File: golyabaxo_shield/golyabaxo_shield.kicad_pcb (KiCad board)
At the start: 2 copper layers, 53.6 x 54 mm, 18 parts, among them J2 Conn_01x09, Q2 Q_NPN_BEC

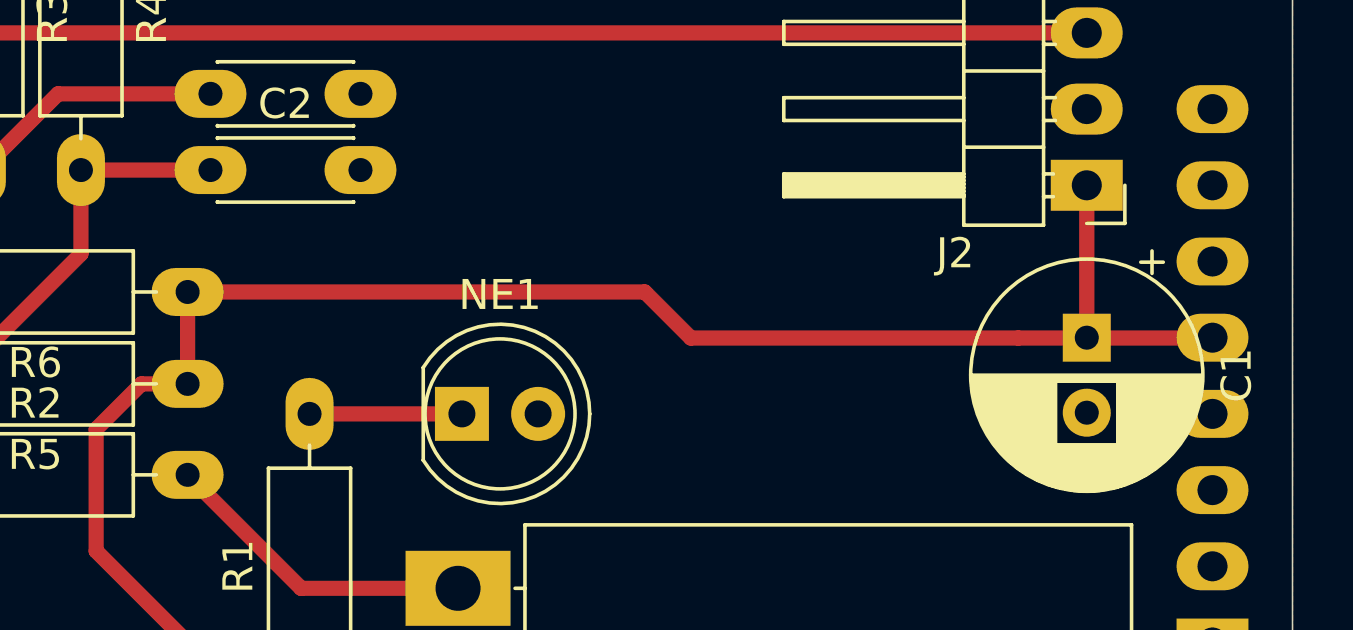
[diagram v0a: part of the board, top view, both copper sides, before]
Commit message: Add refurbished firmware for SEMduino-V2 - testing needed
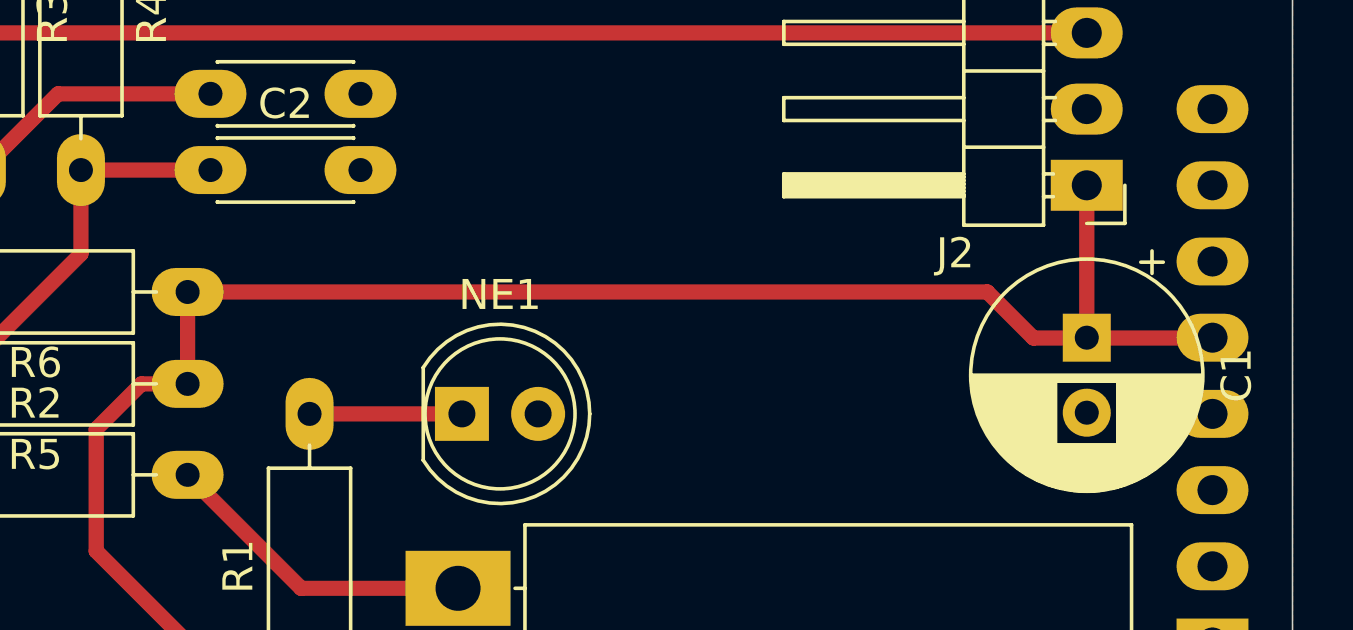
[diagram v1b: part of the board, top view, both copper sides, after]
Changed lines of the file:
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@@
 		(tags "Resistor Axial_DIN0207 series Axial Horizontal pin pitch 10.16mm 0.25W = 1/4W length 6.3mm diameter 2.5mm")
 		(property "Reference" "R1"
-			(at 5.08 -2.37 270)
+			(at 5.08 -2.37 -90)
 			(layer "F.SilkS")
 			(effects
@@
 		)
 		(property "Value" "820k"
-			(at 5.08 2.37 270)
+			(at 5.08 2.37 -90)
 			(layer "F.Fab")
 			(effects
@@
 		)
 		(fp_text user "${REFERENCE}"
-			(at 5.08 0 270)
+			(at 5.08 0 -90)
 			(layer "F.Fab")
 			(effects
@@
 		(tags "C Disc series Radial pin pitch 5.00mm  diameter 4.3mm width 1.9mm Capacitor")
 		(property "Reference" "C3"
-			(at 2.5 -3.724 360)
+			(at 2.5 -3.724 0)
 			(layer "F.SilkS")
 			(effects
@@
 		)
 		(property "Value" "47p"
-			(at 2.5 2.2 360)
+			(at 2.5 2.2 0)
 			(layer "F.Fab")
 			(effects
@@
 		)
 		(fp_text user "${REFERENCE}"
-			(at 2.5 0 360)
+			(at 2.5 0 0)
 			(layer "F.Fab")
 			(effects
@@
 		(tags "C Disc series Radial pin pitch 5.00mm  diameter 4.3mm width 1.9mm Capacitor")
 		(property "Reference" "C2"
-			(at 2.5 -2.2 360)
+			(at 2.5 -2.2 0)
 			(layer "F.SilkS")
 			(effects
@@
 		)
 		(property "Value" "47p"
-			(at 2.5 2.2 360)
+			(at 2.5 2.2 0)
 			(layer "F.Fab")
 			(effects
@@
 		)
 		(fp_text user "${REFERENCE}"
-			(at 2.5 0 360)
+			(at 2.5 0 0)
 			(layer "F.Fab")
 			(effects
@@
 		)
 		(fp_text user "${REFERENCE}"
-			(at 2.77 10.16 270)
+			(at 2.77 10.16 -90)
 			(layer "F.Fab")
 			(effects
@@
 		(tags "Arduino UNO R3")
 		(property "Reference" "A2"
-			(at 1.27 3.81 270)
+			(at 1.27 3.81 -90)
 			(layer "B.SilkS")
 			(effects
@@
 		)
 		(property "Value" "Arduino_UNO_R3"
-			(at 0 -22.86 270)
+			(at 0 -22.86 -90)
 			(layer "B.Fab")
 			(effects
@@
 		)
 		(fp_text user "${REFERENCE}"
-			(at 0 -20.32 270)
+			(at 0 -20.32 -90)
 			(layer "B.Fab")
 			(effects
@@
 	)
 	(segment
-		(start 131.953 87.492002)
-		(end 147.193 87.492002)
-		(width 0.508)
-		(layer "F.Cu")
-		(net 16)
-	)
-	(segment
 		(start 161.925 83.936002)
 		(end 161.925 89.016002)
@@
 	)
 	(segment
-		(start 148.727998 89.027)
-		(end 159.639 89.027)
+		(start 131.953 87.492002)
+		(end 158.612002 87.492002)
 		(width 0.508)
 		(layer "F.Cu")
@@
 	)
 	(segment
-		(start 147.193 87.492002)
-		(end 148.727998 89.027)
+		(start 158.612002 87.492002)
+		(end 160.147 89.027)
 		(width 0.508)
 		(layer "F.Cu")
@@
 	)
 	(segment
-		(start 166.116 89.027)
-		(end 159.639 89.027)
+		(start 130.413 90.556002)
+		(end 131.953 90.556002)
 		(width 0.508)
 		(layer "F.Cu")
@@
 	)
 	(segment
-		(start 130.413 90.556002)
-		(end 131.953 90.556002)
+		(start 160.147 89.027)
+		(end 166.116 89.027)
 		(width 0.508)
 		(layer "F.Cu")

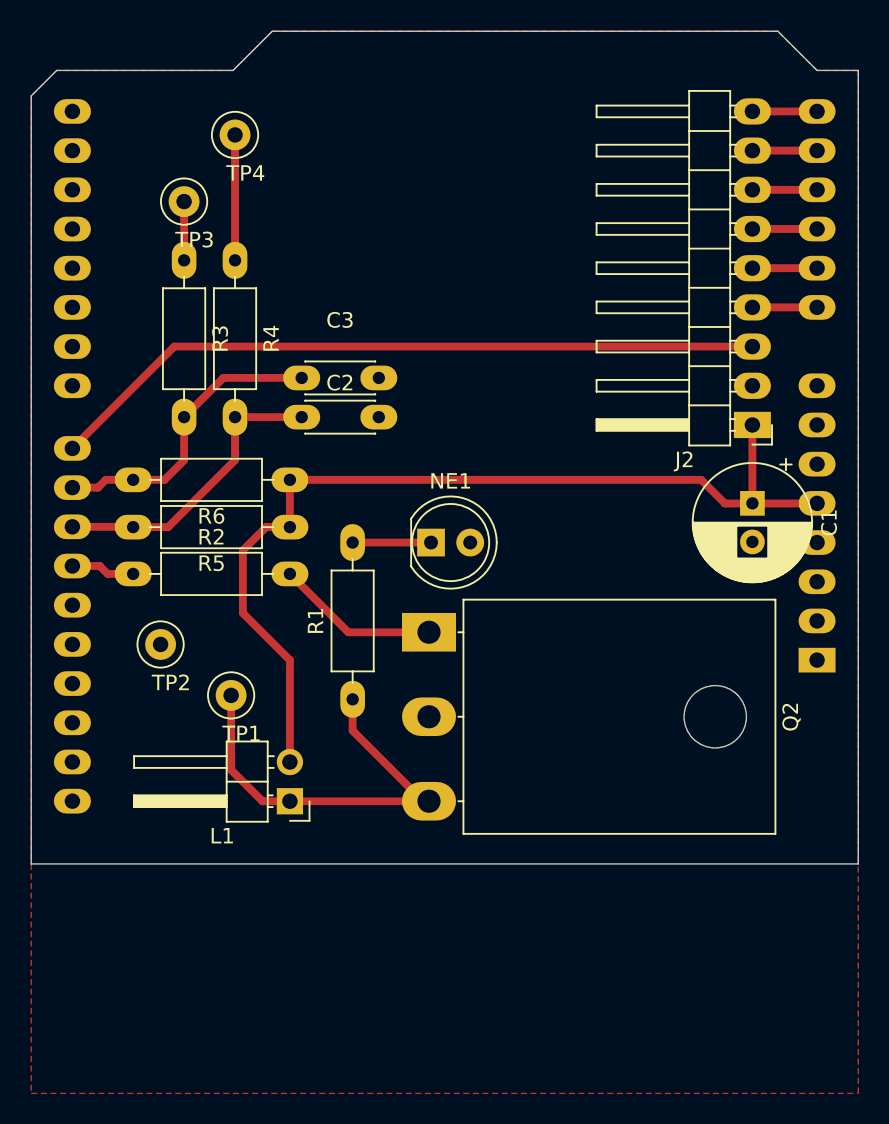
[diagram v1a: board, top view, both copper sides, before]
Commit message: Build SEMduino shield
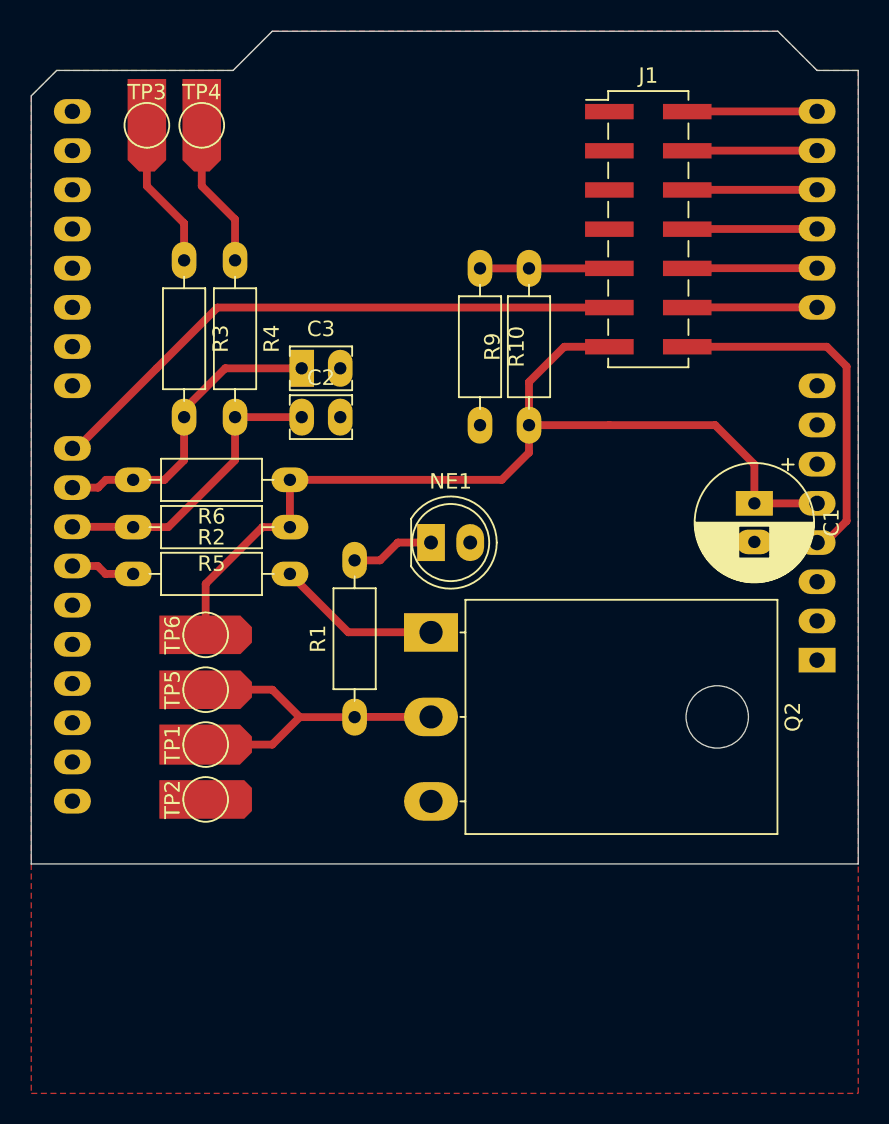
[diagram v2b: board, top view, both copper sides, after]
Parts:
- removed J2: Conn_01x09, Connector_PinHeader_2.54mm:PinHeader_1x09_P2.54mm_Horizontal
- removed L1: 22.5mH, Connector_PinHeader_2.54mm:PinHeader_1x02_P2.54mm_Horizontal
- added J1: Conn_02x07_Odd_Even, Connector_PinHeader_2.54mm:PinHeader_2x07_P2.54mm_Vertical_SMD, F.Cu at (155.2, 71.2)
- added R10: 1k2, Resistor_THT:R_Axial_DIN0207_L6.3mm_D2.5mm_P10.16mm_Horizontal, F.Cu at (144.3, 73.8)
- added R9: 3k3, Resistor_THT:R_Axial_DIN0207_L6.3mm_D2.5mm_P10.16mm_Horizontal, F.Cu at (147.4, 83.9)
- added TP5: Tekercs, TestPoint:TestPoint_Pad_D2.5mm, F.Cu at (126.5, 101.1)
- added TP6: Tekercs, TestPoint:TestPoint_Pad_D2.5mm, F.Cu at (126.5, 97.5)
- A2: value Arduino_UNO_R3 -> SEMDUINO_V2
- C2, C3: value 47p -> 47n; footprint Capacitor_THT:C_Disc_D4.3mm_W1.9mm_P5.00mm -> Capacitor_THT:C_Disc_D3.8mm_W2.6mm_P2.50mm
- NE1: footprint LED_THT:LED_D5.0mm_Clear -> LED_THT:LED_D5.0mm_IRGrey
- Q2: value Q_NPN_BEC -> BUV48A
- TP1, TP2, TP3, TP4: footprint TestPoint:TestPoint_Loop_D2.50mm_Drill1.0mm -> TestPoint:TestPoint_Pad_D2.5mm
- moved TP2 10.5 mm to (126.5, 108.2), turned to 90 degrees
- moved TP3 5.50 mm to (122.7, 64.5)
- moved TP1 3.59 mm to (126.5, 104.6), turned to 90 degrees
- moved TP4 2.25 mm to (126.2, 64.5)
- moved R1 1.16 mm to (136.1, 102.9)
- moved C3 0.62 mm to (132.7, 80.3)
- moved Q2 0.13 mm to (141.1, 97.4)
- moved C1 0.13 mm to (162.1, 89.0)
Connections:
- A2 pad 10: /LCD_D1 -> /LCD_D5
- A2 pad 11: /LCD_D2 -> /LCD_D6
- A2 pad 12: /LCD_D3 -> /LCD_D7
- A2 pad 19: /??? -> unconnected-(A2-D4-Pad19)
- A2 pad 4: unconnected-(A2-3V3-Pad4) -> +3V3
- A2 pad 9: /LCD_D0 -> /LCD_D4
- Q2 pad 2: GND -> Net-(Q2-C-Pad2)
- Q2 pad 3: Net-(Q2-C) -> GND
- R1 pad 1: Net-(Q2-C) -> Net-(Q2-C-Pad2)
- TP1 pad 1: Net-(Q2-C) -> Net-(Q2-C-Pad2)
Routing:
- net Net-(Q2-C): track 27.4 -> 0.00 mm
- net +3V3: track 0.00 -> 23.4 mm
- net Net-(Q2-C-Pad2): track 0.00 -> 22.2 mm
- net /LCD_D7: track 0.00 -> 8.42 mm
- net /LCD_D6: track 0.00 -> 8.42 mm
- net /LCD_D5: track 0.00 -> 8.42 mm
- net /LCD_D4: track 0.00 -> 8.42 mm
- net /LCD_V0: track 0.00 -> 8.38 mm
- net /LCD_E: track 46.8 -> 38.6 mm
- net Net-(R3-Pad1): track 3.81 -> 9.75 mm
- net /LCD_RW: track 4.19 -> 8.42 mm
- net /LCD_RS: track 4.19 -> 8.42 mm
- net /LCD_D3: track 4.19 -> 0.00 mm
- net /LCD_D2: track 4.19 -> 0.00 mm
- net /LCD_D1: track 4.19 -> 0.00 mm
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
